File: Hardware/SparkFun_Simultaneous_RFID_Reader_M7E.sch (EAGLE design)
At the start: 41 parts, among them J5 U.FL, U1 UHF_RFID_NANO_MODULE_M7E_HECTO, U2 CH340C

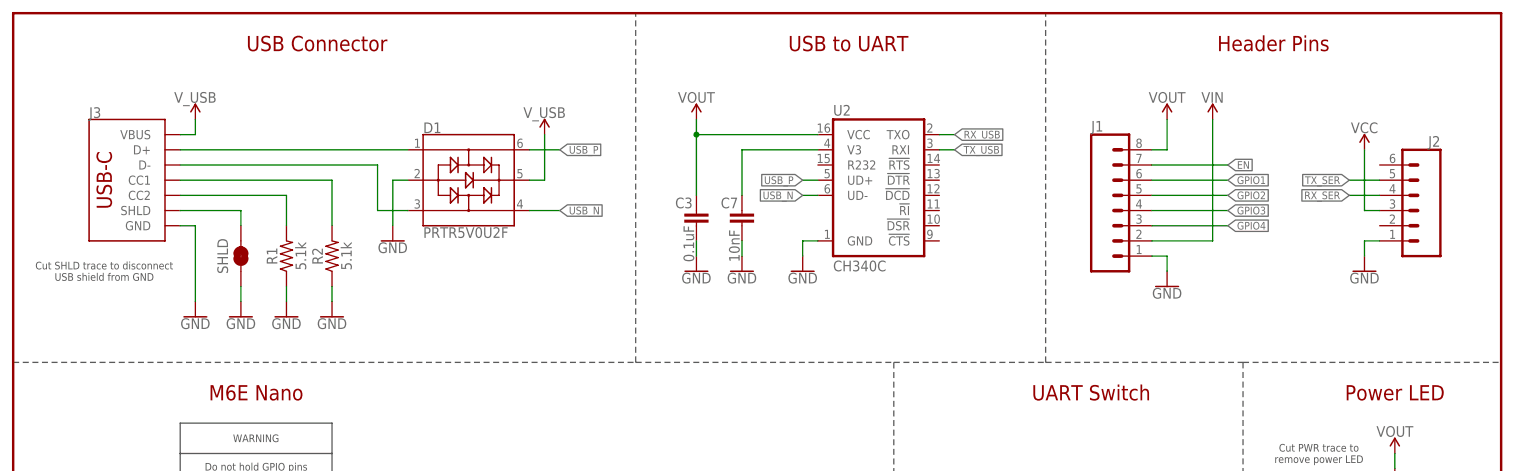
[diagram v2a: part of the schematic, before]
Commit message: Fix CH340 power
Can't be powered by VOUT, because the module outputs 2.5V while idle, which is too low for the CH340
Now powered by VUSB.  The only problem here is that the output voltage is based on VCC, so a voltage divider is used to make the output voltage ~3.3V
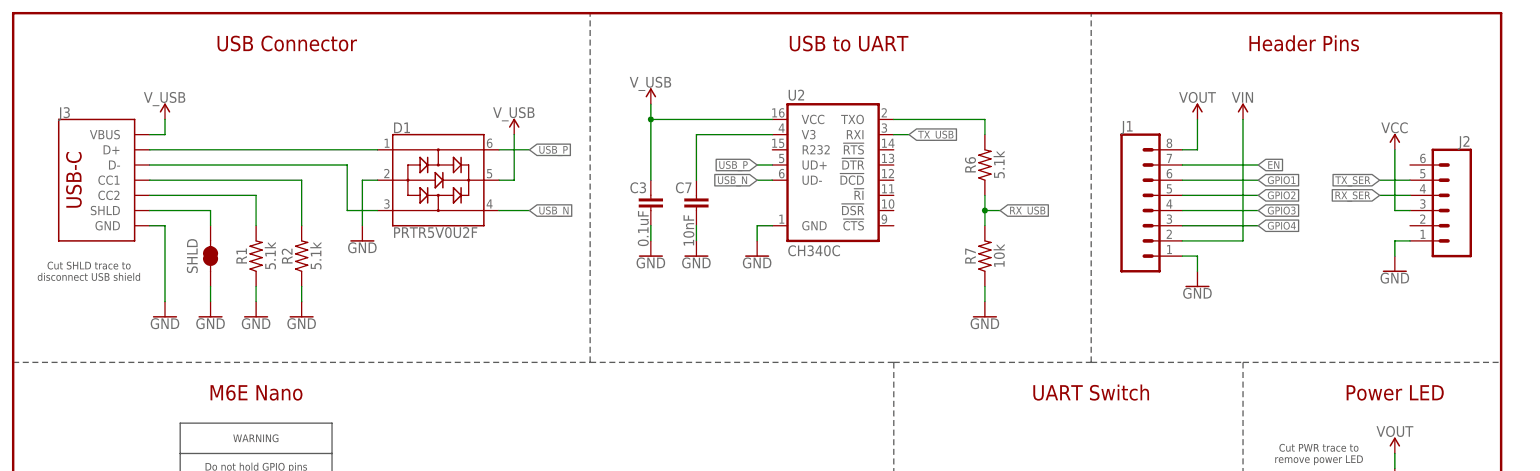
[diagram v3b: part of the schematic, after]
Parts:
- added R6: 5.1k, SparkFun-Resistors:5.1KOHM5.1KOHM-0603-1/10W-1%
- added R7: 10k, SparkFun-Resistors:10KOHM-0603-1/10W-1%
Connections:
- new net N$14: R6.2, U2.TXO
- net GND: now also R7.1
- net RX_USB: now also R6.1, R7.2; no longer U2.TXO
- net VOUT: no longer C3.1, U2.VCC
- net V_USB: now also C3.1, U2.VCC
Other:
- note added: "Cut SHLD trace to disconnect USB shield"
- note removed: "Cut SHLD trace to disconnect USB shield from GND"
- moved on the sheet: C3, C7, D1, J1, J2, J3, R1, R2, SHLD, U2
